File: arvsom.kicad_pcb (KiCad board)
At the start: 12 copper layers, 55 x 40 mm, 412 parts, among them J1 TAG-10PIN, J3 DF40C-100DP-0.4V(51), J4 DF40C-100DP-0.4V(51), Q1 DMG1013UWQ-7, Q5 DMG1012UW, U1 MT53D1024M32D4DT-053, U10 TDA19988BHN_C1,557, U11 KSZ9031RNXCA, U13 VIC7100, U2 GD25LQ256DWIGR, U3 MT53D1024M32D4DT-053, U4 CSD86330Q3D, U5 LMR62014XMF_NOPB, U6 CSD86330Q3D, U7 STM811RW16F, U8 TPS65086100, Y1 ABM8G-25.000MHZ-18-D2Y-T, Y2 ABM8G-25.000MHZ-18-D2Y-T, Y3 ABM8G-27.000MHZ-18-D2Y-T

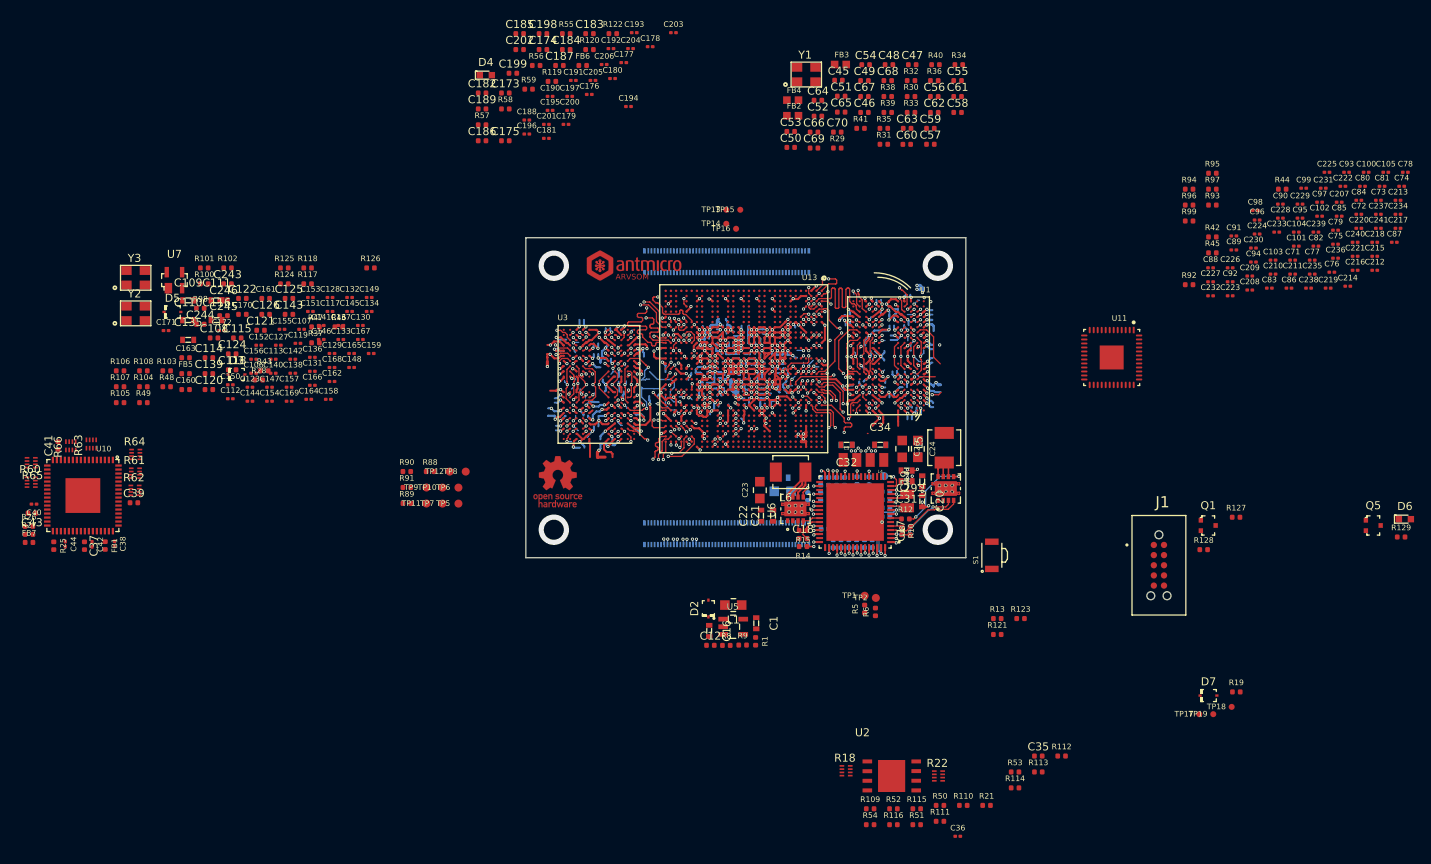
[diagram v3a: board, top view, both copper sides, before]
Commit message: Updated component placement - PHY passives placed, moved HDMI IC, lowered VIC and DDRs
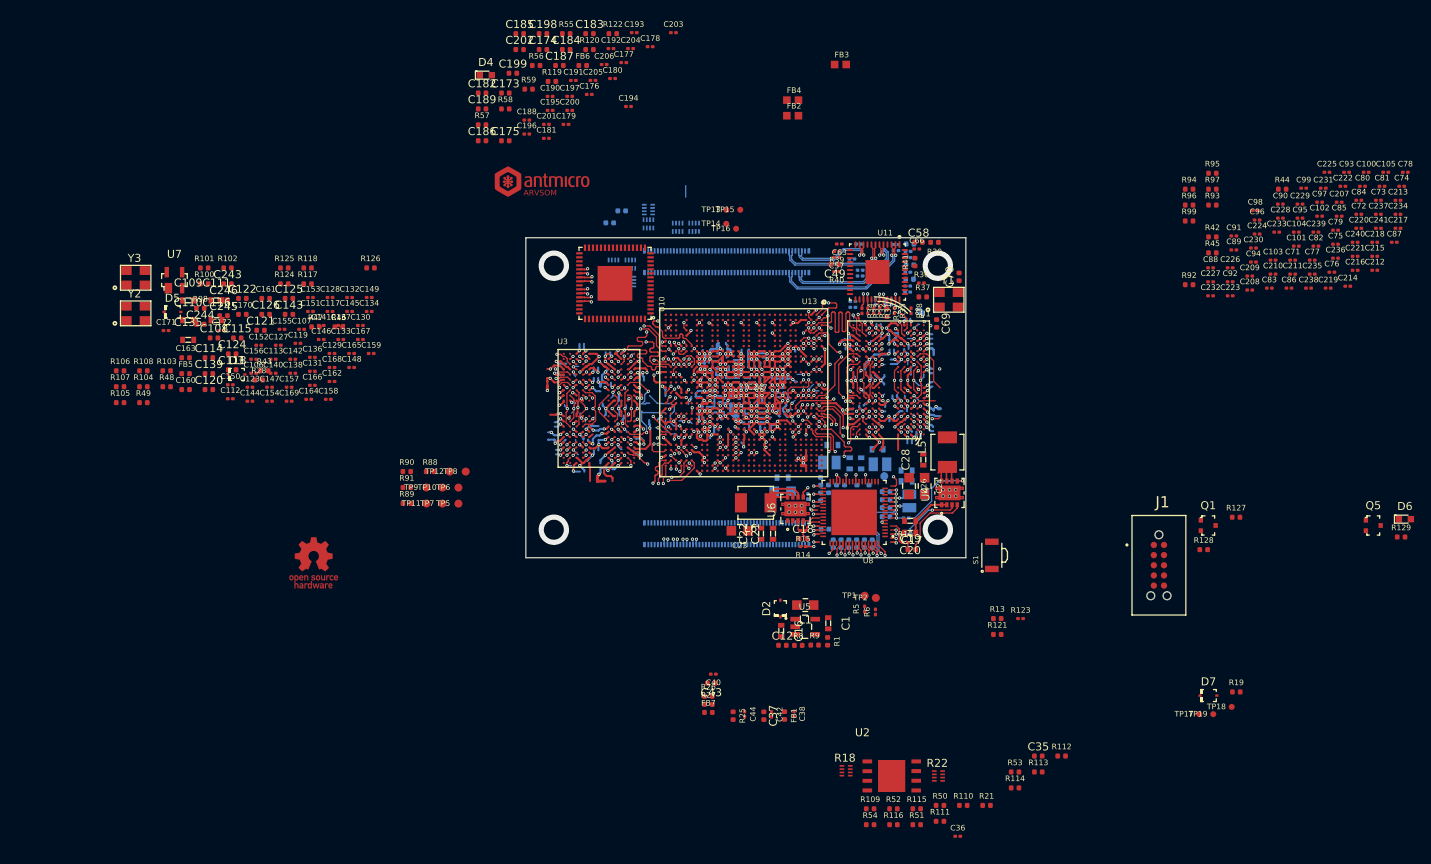
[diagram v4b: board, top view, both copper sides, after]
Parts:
- added C247: C_100n_0201, arvsom-footprints:0201-res, F.Cu at (159.0, 74.7)
- C28: moved to F.Cu
- C29, C31, C32, C34, C39, C41, C45, C47, C50, L2, L3, L4, R60, R61, R62, R63, R64, R65, R66: moved to B.Cu
- C46, C48, C51, C52, C53: value C_470n_0402 -> C_470n_0201; footprint arvsom-footprints:0402-cap -> arvsom-footprints:0201-res; moved to B.Cu
- C54: value C_100n_0402 -> C_100n_0201; footprint arvsom-footprints:0402-cap -> arvsom-footprints:0201-res; moved to B.Cu
- C55, C56, C59, C60, C61, C62, C64, C65, C67, C68: value C_10n_0402 -> C_10n_0201; footprint arvsom-footprints:0402-cap -> arvsom-footprints:0201-res; moved to B.Cu
- C57, C63, C66: value C_10n_0402 -> C_10n_0201; footprint arvsom-footprints:0402-cap -> arvsom-footprints:0201-res
- R10, R11, R123, R14, R15, R16, R5, R6: value R_0R_0402 -> R_0R_0201; footprint arvsom-footprints:0402-res -> antmicro-footprints:0201-res
- R12: value R_0R_0402 -> R_0R_0201; footprint arvsom-footprints:0402-res -> antmicro-footprints:0201-res; moved to B.Cu
- R31, R32, R33, R34, R35, R36, R38, R39, R40: value R_10k_0402 -> R_10k_0201; footprint arvsom-footprints:0402-res -> arvsom-footprints:0201-res
- U8: footprint arvsom-footprints:QFN50P900X900X80-65N -> arvsom-footprints:S-PVQFN-N64
- moved C37 87.5 mm to (159.8, 114.7)
- moved FB1 87.5 mm to (162.4, 114.7)
- moved R26 87.5 mm to (152.8, 112.3)
- moved C38 87.5 mm to (163.5, 114.5)
- moved C40 87.5 mm to (153.5, 109.5)
- moved C42 87.5 mm to (160.7, 114.5)
- moved C44 87.5 mm to (157.4, 114.5)
- moved FB7 87.5 mm to (152.8, 114.3)
- moved R25 87.5 mm to (155.9, 114.7)
- moved R27 87.5 mm to (152.8, 113.3)
- moved C43 87.5 mm to (153.2, 110.7)
- moved R65 78.9 mm to (143.1, 58.3), turned to 270 degrees
- moved R60 77.7 mm to (141.0, 58.3), turned to 270 degrees
- moved C41 76.3 mm to (142.0, 51.6), turned to 180 degrees
- moved R61 76.3 mm to (151.0, 53.7), turned to 270 degrees
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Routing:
- net HDMI_TXC_N: track 23.5 -> 4.91 mm, vias 1 -> 2
- net HDMI_TXC_P: track 23.5 -> 5.47 mm, vias 1 -> 2
- net ETH0_P: track 0.00 -> 18.0 mm, vias 0 -> 1
- net ETH0_N: track 0.00 -> 17.2 mm, vias 0 -> 1
- net ETH1_N: track 0.00 -> 17.2 mm, vias 0 -> 1
- net HDMI_TX0_N: track 23.3 -> 7.14 mm, vias 1 -> 2
- net ETH1_P: track 0.00 -> 15.7 mm, vias 0 -> 1
- net HDMI_TX0_P: track 23.3 -> 7.70 mm, vias 1 -> 2
- net (no net): track 0.00 -> 15.6 mm
- net HDMI_TX1_N: track 23.3 -> 7.91 mm, vias 1 -> 2
- net HDMI_TX1_P: track 23.3 -> 8.46 mm, vias 1 -> 2
- net ETH2_P: track 0.00 -> 14.2 mm, vias 0 -> 1
- net ETH2_N: track 0.00 -> 13.4 mm, vias 0 -> 1
- net HDMI_TX2_N: track 22.8 -> 9.62 mm, vias 1 -> 2
- net HDMI_TX2_P: track 23.0 -> 10.2 mm, vias 1 -> 2
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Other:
- net class eth added: clearance 0.1, trace_width 0.127, via_dia 0.4, via_drill 0.2

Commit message: Updated component placement - HDMI IC passives, QSPI, 5V8 buck placed
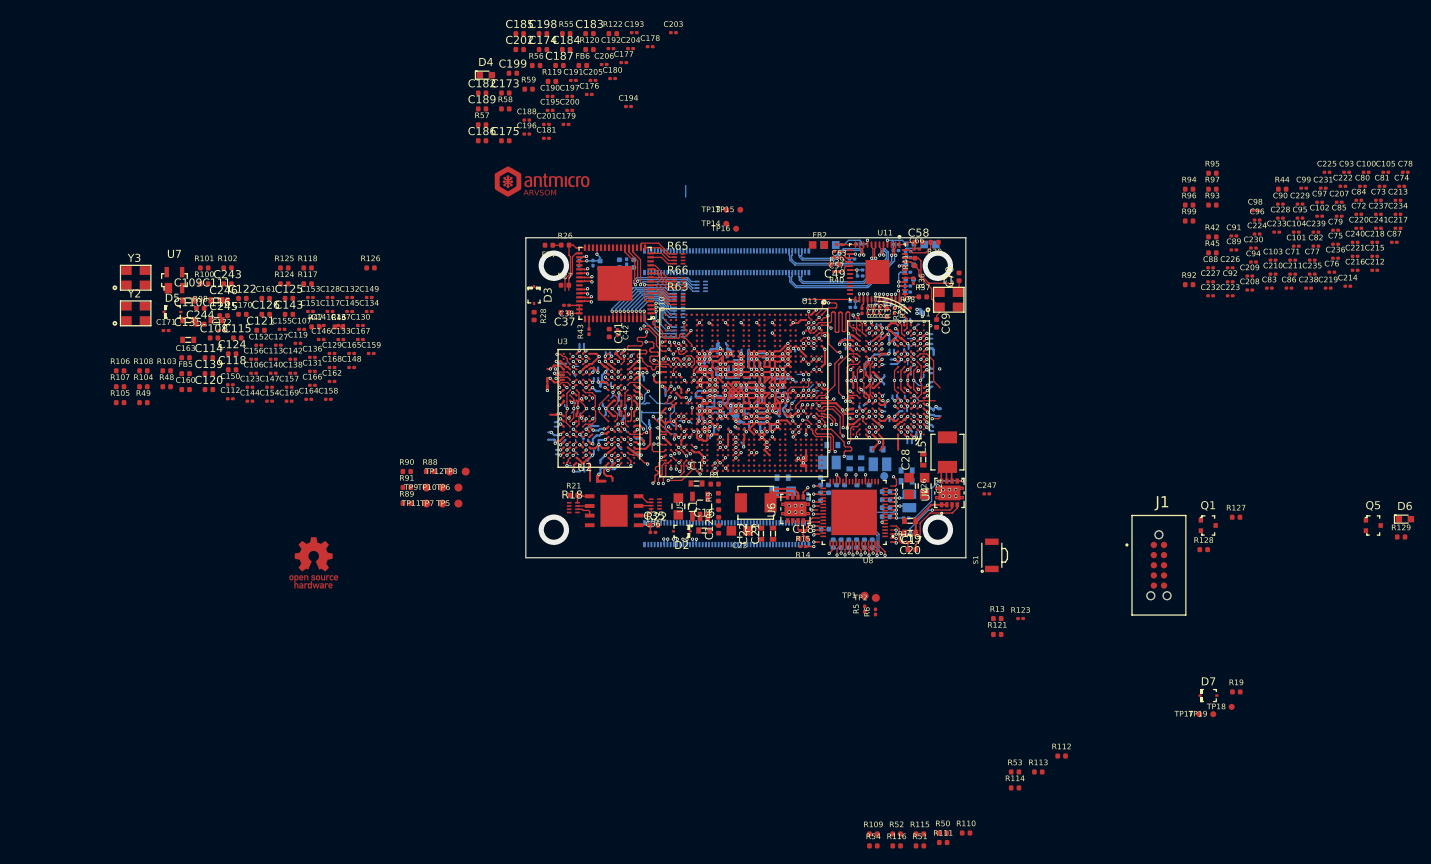
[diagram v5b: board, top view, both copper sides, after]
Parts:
- C40, C43, C44, FB1, FB3, FB4: moved to B.Cu
- C41, R63, R65, R66: moved to F.Cu
- R25: value R_10k_0402 -> R_10k_0201; footprint arvsom-footprints:0402-res -> arvsom-footprints:0201-res; moved to B.Cu
- R43: value R_10k_0402 -> R_10k_0201; footprint arvsom-footprints:0402-res -> arvsom-footprints:0201-res
- moved R21 64.5 mm to (136.0, 87.2)
- moved FB7 61.7 mm to (132.9, 55.9), turned to 180 degrees
- moved R25 59.8 mm to (136.7, 58.2), turned to 90 degrees
- moved FB1 59.6 mm to (143.5, 58.2)
- moved R26 59.2 mm to (134.9, 55.9)
- moved C38 58.4 mm to (135.1, 63.4), turned to 180 degrees
- moved C44 58.4 mm to (142.6, 58.0)
- moved C37 56.2 mm to (134.9, 64.3), turned to 180 degrees
- moved C35 56.0 mm to (146.1, 90.9)
- moved R27 55.4 mm to (134.9, 60.9)
- moved C36 53.8 mm to (145.9, 91.8)
- moved C43 53.7 mm to (141.7, 58.2), turned to 270 degrees
- moved C40 53.5 mm to (138.4, 58.1), turned to 270 degrees
- moved C42 51.5 mm to (141.5, 66.8)
- moved R22 49.1 mm to (146.2, 88.3), turned to 180 degrees
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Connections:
- R22 pad 1: Net-(R22-Pad1) -> QSPI_D3
- R22 pad 2: Net-(R22-Pad2) -> QSPI_CLK
- R22 pad 3: Net-(R22-Pad3) -> QSPI_D0
- R22 pad 6: QSPI_D0 -> Net-(R22-Pad6)
- R22 pad 7: QSPI_CLK -> Net-(R22-Pad7)
- R22 pad 8: QSPI_D3 -> Net-(R22-Pad8)
- R25 pad 1: HDMI_SWING -> GND
- R25 pad 2: GND -> HDMI_SWING
- R64 pad 1: LCD_DATA12 -> Net-(R64-Pad1)
- R64 pad 2: LCD_DATA13 -> Net-(R64-Pad2)
- R64 pad 3: LCD_DATA14 -> Net-(R64-Pad3)
- R64 pad 4: LCD_DATA15 -> Net-(R64-Pad4)
- R64 pad 5: Net-(R64-Pad5) -> LCD_DATA15
- R64 pad 6: Net-(R64-Pad6) -> LCD_DATA14
- R64 pad 7: Net-(R64-Pad7) -> LCD_DATA13
- R64 pad 8: Net-(R64-Pad8) -> LCD_DATA12
- U13 pad AD2: Net-(R64-Pad5) -> Net-(R64-Pad4)
- U13 pad AE1: Net-(R64-Pad6) -> Net-(R64-Pad3)
- U13 pad AG3: Net-(R64-Pad7) -> Net-(R64-Pad2)
- U2 pad 5: (no net) -> Net-(R22-Pad6)
- U2 pad 6: Net-(R22-Pad2) -> Net-(R22-Pad7)
- U2 pad 7: Net-(R22-Pad1) -> Net-(R22-Pad8)
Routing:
- net LCD_HSYNC: track 0.00 -> 14.0 mm, vias 0 -> 1
- net LCD_DE: track 0.00 -> 12.5 mm, vias 0 -> 1
- net LCD_VSYNC: track 0.00 -> 12.4 mm, vias 0 -> 1
- net VCC_1V2: track 0.00 -> 11.8 mm, vias 0 -> 5
- net HDMI_TXC_N: track 4.91 -> 16.7 mm
- net Net-(C70-Pad1): track 0.00 -> 11.0 mm
- net HDMI_TXC_P: track 5.47 -> 16.5 mm
- net HDMI_TX0_N: track 7.14 -> 18.1 mm
- net LCD_DATA7: track 0.00 -> 10.9 mm, vias 0 -> 1
- net HDMI_TX0_P: track 7.70 -> 17.7 mm
- net /Ethernet/AVDDL: track 0.00 -> 9.88 mm, vias 0 -> 2
- net LCD_DATA6: track 0.00 -> 9.85 mm, vias 0 -> 1
- net LCD_PCLK: track 0.00 -> 9.63 mm, vias 0 -> 1
- net Net-(C69-Pad1): track 0.00 -> 9.59 mm
- net LCD_DATA5: track 0.00 -> 9.33 mm, vias 0 -> 1
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
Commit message: Updated component placement - VIC power decoupling done
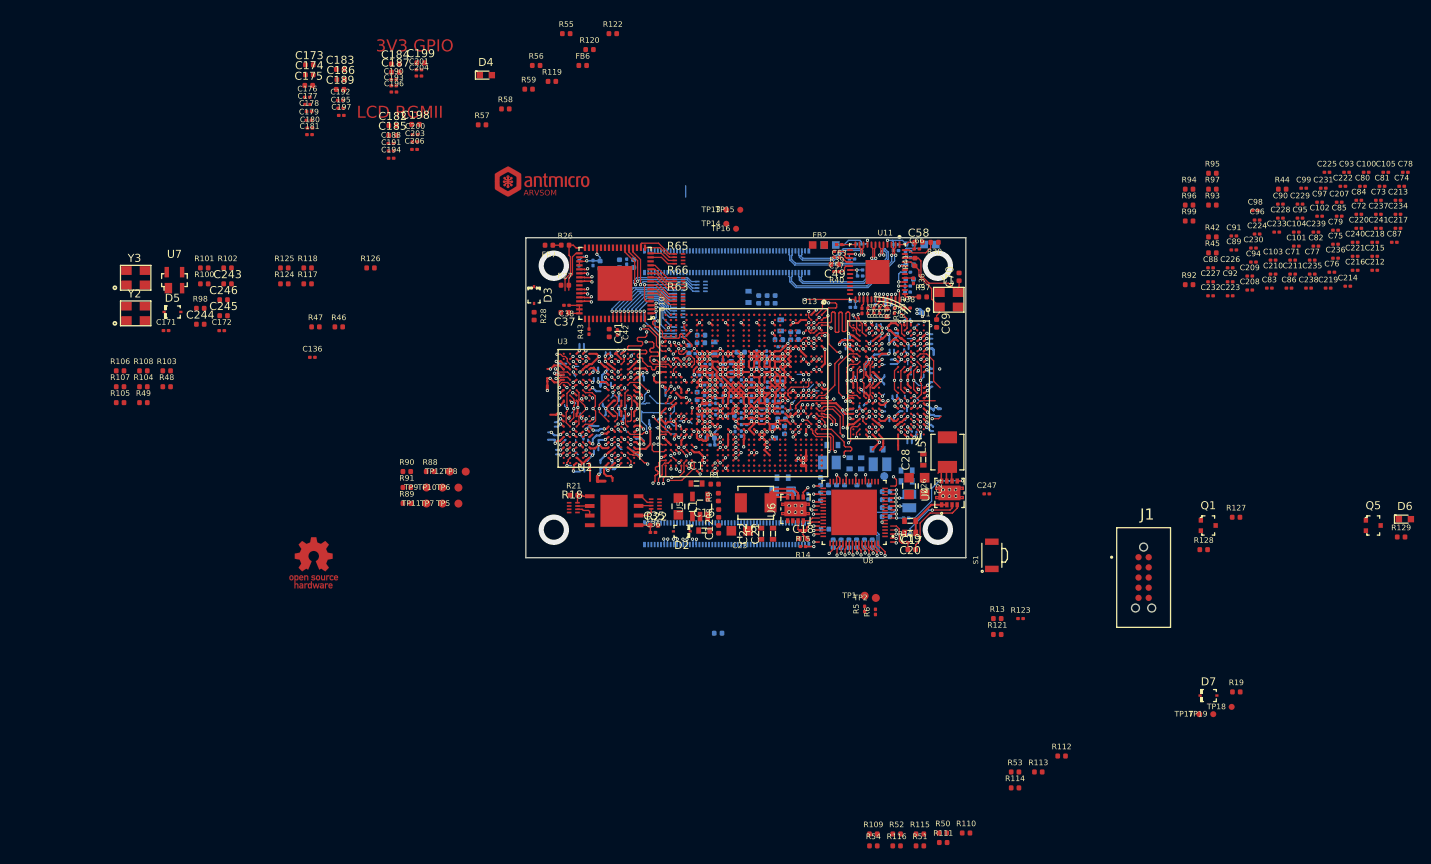
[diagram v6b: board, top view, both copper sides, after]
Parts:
- C106, C107, C108, C109, C110, C111, C112, C113, C114, C115, C116, C117, C118, C119, C120, C121, C122, C123, C124, C125, C126, C127, C128, C129, C130, C131, C132, C133, C134, C135, C137, C138, C139, C140, C141, C142, C143, C144, C145, C146, C147, C148, C149, C150, C151, C152, C153, C154, C155, C156, C157, C158, C159, C160, C161, C162, C163, C164, C165, C166, C167, C168, C169, C170, C202, C205, FB5: moved to B.Cu
- moved C110 74.1 mm to (161.9, 65.9), turned to 90 degrees
- moved FB5 74.1 mm to (154.1, 104.4)
- moved C163 72.0 mm to (159.1, 62.7), turned to 90 degrees
- moved C111 71.7 mm to (161.1, 79.3), turned to 270 degrees
- moved C139 71.4 mm to (161.2, 62.7), turned to 90 degrees
- moved C135 70.3 mm to (157.9, 62.4), turned to 90 degrees
- moved C122 69.7 mm to (162.4, 79.0), turned to 270 degrees
- moved C150 68.7 mm to (161.8, 74.7)
- moved C112 68.2 mm to (161.3, 75.4)
- moved C115 67.7 mm to (161.7, 67.7), turned to 180 degrees
- moved C121 66.1 mm to (162.0, 77.6)
- moved C109 66.0 mm to (153.6, 68.7), turned to 90 degrees
- moved C170 66.0 mm to (159.7, 75.3), turned to 180 degrees
- moved C161 65.8 mm to (163.1, 67.2), turned to 90 degrees
- moved C108 65.3 mm to (155.6, 77.2), turned to 180 degrees
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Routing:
- net GND: track 411.3 -> 339.4 mm, vias 236 -> 235
- net VCC_1V1: track 182.5 -> 158.9 mm, vias 110 -> 105
- net VCC_0V9: track 60.8 -> 41.0 mm
- net VCC_3V3: track 35.6 -> 25.5 mm
- net VCC_1V8: track 63.8 -> 55.2 mm, vias 29 -> 28
- net AVDD09_PLL: track 8.38 -> 1.38 mm, vias 2 -> 1
- net AVDD3V3_USB: track 1.03 -> 3.09 mm
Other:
- board text added: "3V3 GPIO"
- board text added: "LCD RGMII"
